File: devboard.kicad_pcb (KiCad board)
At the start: 4 copper layers, 132.1 x 62.2 mm, 91 parts, among them J1 Conn_01x04, J2 Conn_02x05_Odd_Even, J3 USB_B_Micro, J4 Conn_01x04, J5 Conn_02x10_Counter_Clockwise, J6 Conn_02x04_Counter_Clockwise, Q1 Q_NPN_BEC, Q2 Q_NPN_BEC, SW1 SW_SPST, U1 ATmega128L-8AU, U10 FT232RL, U2 MAX6371, U3 CY62158EV30LL-45ZSXIT, U4 AP2112K-3.3, U5 CY62158EV30LL-45ZSXIT, U6 CY62158EV30LL-45ZSXIT, U7 CY62158EV30LL-45ZSXIT, U8 CY62158EV30LL-45ZSXIT, U9 CY62158EV30LL-45ZSXIT

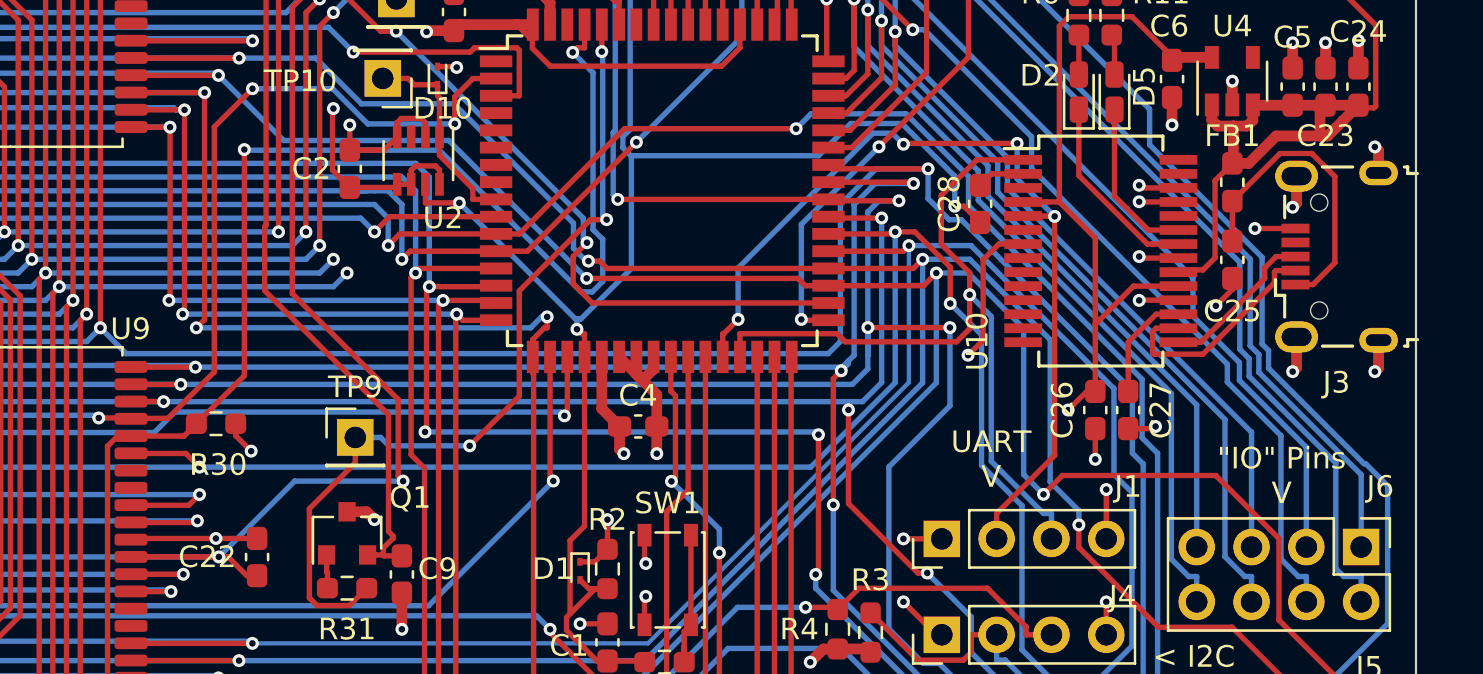
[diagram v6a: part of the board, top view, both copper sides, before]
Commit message: Slight via improvements
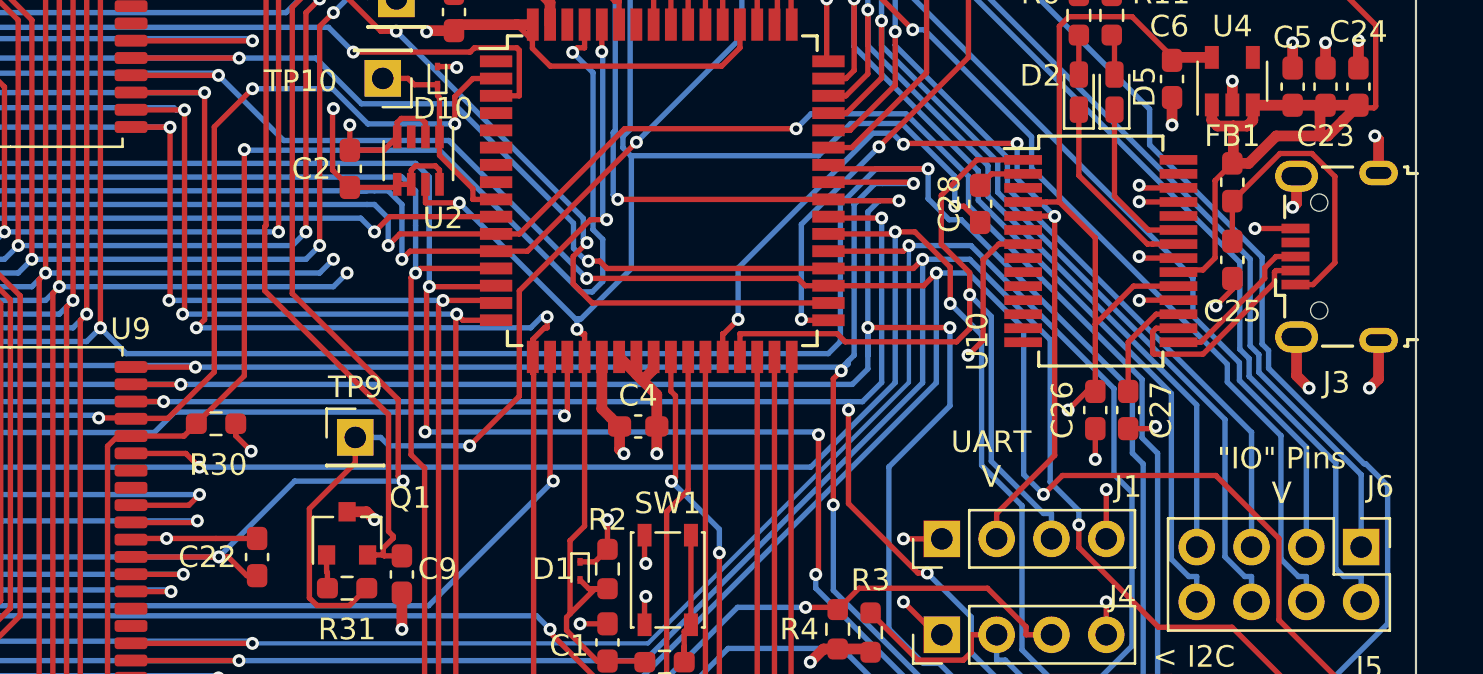
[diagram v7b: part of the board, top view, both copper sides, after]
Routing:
- net GND: track 245.0 -> 247.3 mm
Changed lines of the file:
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@@
     (thickness 1.6)
     (drawings 12)
-    (tracks 2785)
+    (tracks 2786)
     (zones 0)
     (modules 91)
@@
   (layers
     (0 F.Cu signal)
-    (1 In1.Cu signal hide)
-    (2 In2.Cu signal hide)
-    (31 B.Cu signal hide)
-    (32 B.Adhes user hide)
-    (33 F.Adhes user hide)
-    (34 B.Paste user hide)
-    (35 F.Paste user hide)
+    (1 In1.Cu signal)
+    (2 In2.Cu signal)
+    (31 B.Cu signal)
+    (32 B.Adhes user)
+    (33 F.Adhes user)
+    (34 B.Paste user)
+    (35 F.Paste user)
     (36 B.SilkS user)
     (37 F.SilkS user)
-    (38 B.Mask user hide)
-    (39 F.Mask user hide)
-    (40 Dwgs.User user hide)
-    (41 Cmts.User user hide)
-    (42 Eco1.User user hide)
-    (43 Eco2.User user hide)
-    (44 Edge.Cuts user hide)
-    (45 Margin user hide)
+    (38 B.Mask user)
+    (39 F.Mask user)
+    (40 Dwgs.User user)
+    (41 Cmts.User user)
+    (42 Eco1.User user)
+    (43 Eco2.User user)
+    (44 Edge.Cuts user)
+    (45 Margin user)
     (46 B.CrtYd user)
     (47 F.CrtYd user)
-    (48 B.Fab user hide)
-    (49 F.Fab user hide)
+    (48 B.Fab user)
+    (49 F.Fab user)
   )
   (setup
-    (last_trace_width 0.2)
+    (last_trace_width 0.5)
     (user_trace_width 0.2)
     (user_trace_width 0.5)
@@
   (segment (start 108.732 31.4316) (end 108.7311 31.4316) (width 0.25) (layer F.Cu) (net 2))
   (segment (start 108.7325 59.3457) (end 108.7325 59.3462) (width 0.25) (layer F.Cu) (net 2))
-  (segment (start 112.667 59.2912) (end 108.787 59.2912) (width 0.25) (layer F.Cu) (net 2))
+  (segment (start 112.667 59.2912) (end 110.3808 59.2912) (width 0.25) (layer F.Cu) (net 2))
   (segment (start 108.787 59.2912) (end 108.7325 59.3457) (width 0.25) (layer F.Cu) (net 2))
   (segment (start 108.7325 59.3457) (end 108.732 59.3462) (width 0.25) (layer F.Cu) (net 2))
@@
   (segment (start 132.95 51.449) (end 132.434 51.9645) (width 0.5) (layer F.Cu) (net 2))
   (segment (start 132.434 51.9645) (end 131.35 50.88) (width 0.5) (layer F.Cu) (net 2))
-  (segment (start 162.742 42.503) (end 162.742 43.76) (width 0.5) (layer F.Cu) (net 2))
-  (segment (start 162.742 43.76) (end 162.56 43.942) (width 0.5) (layer F.Cu) (net 2))
-  (segment (start 166.542 42.353) (end 166.542 41.32) (width 0.5) (layer F.Cu) (net 2))
-  (segment (start 166.542 41.32) (end 166.37 41.148) (width 0.5) (layer F.Cu) (net 2))
-  (segment (start 166.542 50.103) (end 166.542 51.39) (width 0.5) (layer F.Cu) (net 2))
-  (segment (start 166.542 51.39) (end 166.37 51.562) (width 0.5) (layer F.Cu) (net 2))
-  (segment (start 162.742 49.953) (end 162.742 51.38) (width 0.5) (layer F.Cu) (net 2))
-  (segment (start 162.742 51.38) (end 162.56 51.562) (width 0.5) (layer F.Cu) (net 2))
   (segment (start 132.529 59.139) (end 132.529 60.393) (width 0.25) (layer F.Cu) (net 2))
   (segment (start 132.529 60.393) (end 132.588 60.452) (width 0.25) (layer F.Cu) (net 2))
@@
   (via (at 44.704 22.098) (size 0.6) (layers F.Cu B.Cu) (net 2))
   (via (at 72.644 22.098) (size 0.6) (layers F.Cu B.Cu) (net 2))
-  (via (at 112.667 59.2912) (size 0.6) (layers F.Cu B.Cu) (net 2))
   (via (at 100.838 69.596) (size 0.6) (layers F.Cu B.Cu) (net 2))
   (via (at 44.704 49.784) (size 0.6) (layers F.Cu B.Cu) (net 2))
@@
   (via (at 116.84 22.86) (size 0.6) (layers F.Cu B.Cu) (net 2))
   (via (at 121.285 63.5) (size 0.6) (layers F.Cu B.Cu) (net 2))
-  (via (at 162.56 43.942) (size 0.6) (layers F.Cu B.Cu) (net 2))
-  (via (at 166.37 41.148) (size 0.6) (layers F.Cu B.Cu) (net 2))
-  (via (at 166.37 51.562) (size 0.6) (layers F.Cu B.Cu) (net 2))
-  (via (at 162.56 51.562) (size 0.6) (layers F.Cu B.Cu) (net 2))
   (via (at 132.588 60.452) (size 0.6) (layers F.Cu B.Cu) (net 2))
   (via (at 132.588 61.976) (size 0.6) (layers F.Cu B.Cu) (net 2))
@@
   (segment (start 58.6 31.115) (end 58.42 31.295) (width 0.25) (layer F.Cu) (net 2))
   (segment (start 59.69 31.115) (end 58.6 31.115) (width 0.25) (layer F.Cu) (net 2))
+  (via (at 166.37 40.64) (size 0.6) (drill 0.3) (layers F.Cu B.Cu) (net 2))
+  (segment (start 166.542 40.812) (end 166.37 40.64) (width 0.5) (layer F.Cu) (net 2))
+  (segment (start 166.542 42.353) (end 166.542 40.812) (width 0.5) (layer F.Cu) (net 2))
+  (segment (start 162.742 42.503) (end 162.742 43.76) (width 0.5) (layer F.Cu) (net 2))
+  (segment (start 162.742 43.76) (end 162.56 43.942) (width 0.5) (layer F.Cu) (net 2))
+  (via (at 162.56 43.942) (size 0.6) (layers F.Cu B.Cu) (net 2))
+  (via (at 166.116 52.324) (size 0.6) (drill 0.3) (layers F.Cu B.Cu) (net 2))
+  (segment (start 166.542 51.898) (end 166.116 52.324) (width 0.5) (layer F.Cu) (net 2))
+  (segment (start 166.542 50.103) (end 166.542 51.898) (width 0.5) (layer F.Cu) (net 2))
+  (via (at 163.322 52.324) (size 0.6) (drill 0.3) (layers F.Cu B.Cu) (net 2))
+  (segment (start 162.742 51.744) (end 163.322 52.324) (width 0.5) (layer F.Cu) (net 2))
+  (segment (start 162.742 49.953) (end 162.742 51.744) (width 0.5) (layer F.Cu) (net 2))
+  (segment (start 110.3808 59.2912) (end 108.787 59.2912) (width 0.25) (layer F.Cu) (net 2))
+  (via (at 110.3808 59.2912) (size 0.6) (drill 0.3) (layers F.Cu B.Cu) (net 2))
   (segment (start 136.95 35.48) (end 136.95 36.5553) (width 0.25) (layer F.Cu) (net 3))
   (segment (start 126.6029 35.48) (end 127.332 36.2091) (width 0.25) (layer F.Cu) (net 3))

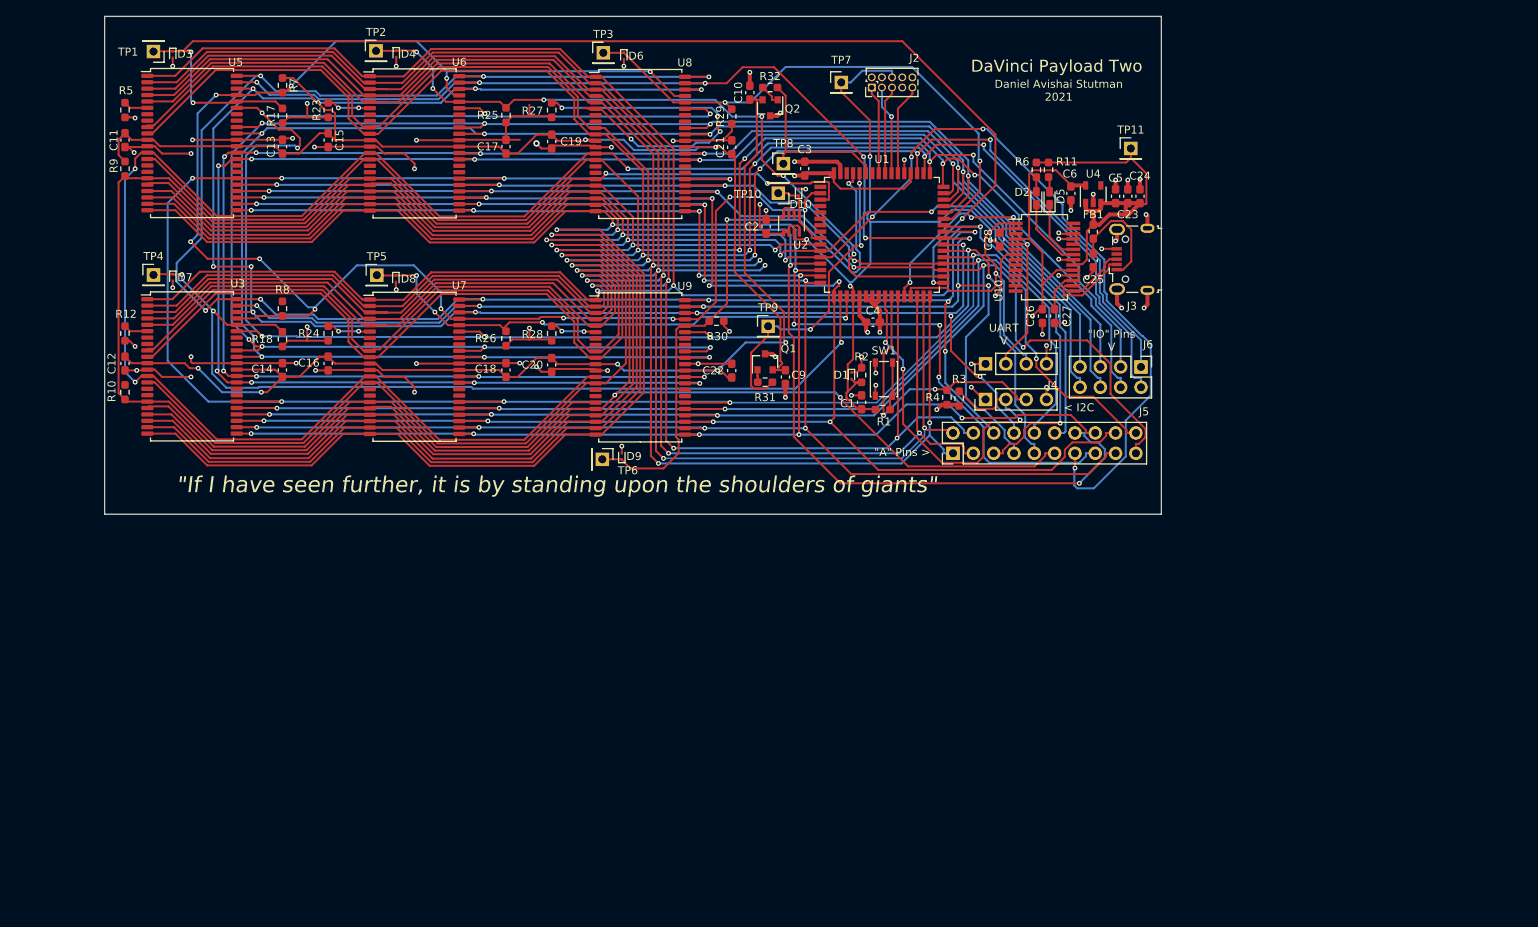
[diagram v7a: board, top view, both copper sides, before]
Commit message: Rounded borders
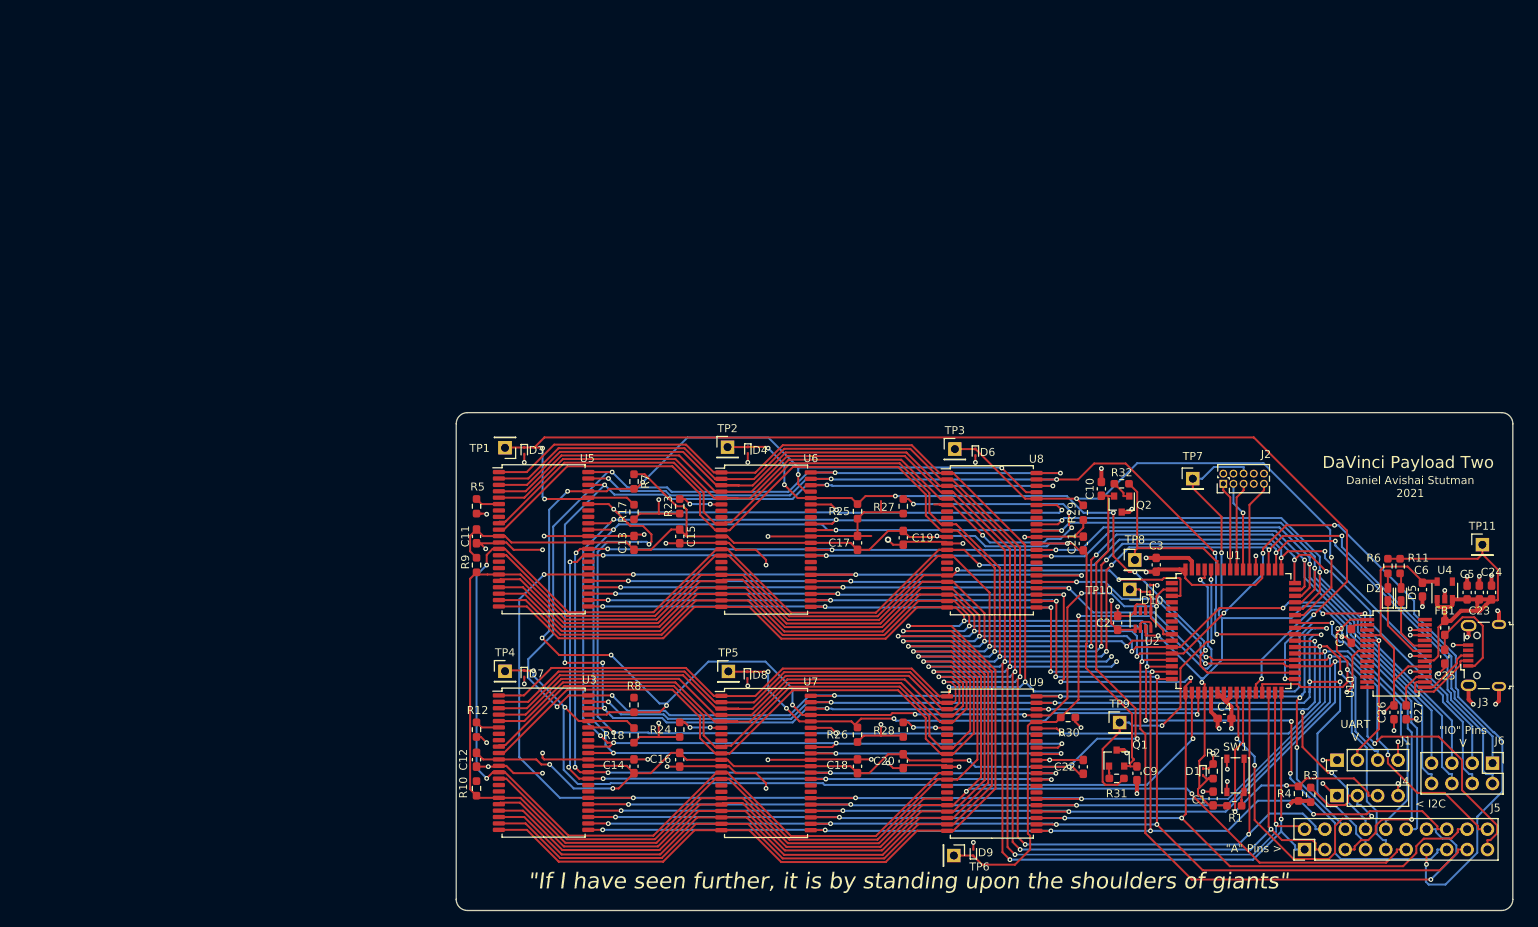
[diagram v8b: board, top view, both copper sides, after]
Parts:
- moved C10 66.2 mm to (160.8, 74.9)
- moved C11 66.2 mm to (82.7, 80.9)
- moved C16 66.2 mm to (108.1, 108.8)
- moved C18 66.2 mm to (130.3, 109.6)
- moved C23 66.2 mm to (208.0, 87.9)
- moved C24 66.2 mm to (209.6, 87.9)
- moved C25 66.2 mm to (203.7, 95.9)
- moved C26 66.2 mm to (198.9, 102.9)
- moved C27 66.2 mm to (197.4, 102.9)
- moved C28 66.2 mm to (192.0, 93.3)
- moved C5 66.2 mm to (206.5, 87.9)
- moved D1 66.2 mm to (173.5, 110.3)
- moved D2 66.2 mm to (196.6, 88.1)
- moved D5 66.2 mm to (198.2, 88.1)
- moved D9 66.2 mm to (144.8, 120.4)
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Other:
- outline, holes or cut-outs redrawn
